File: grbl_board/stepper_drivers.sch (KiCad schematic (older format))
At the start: 44 parts

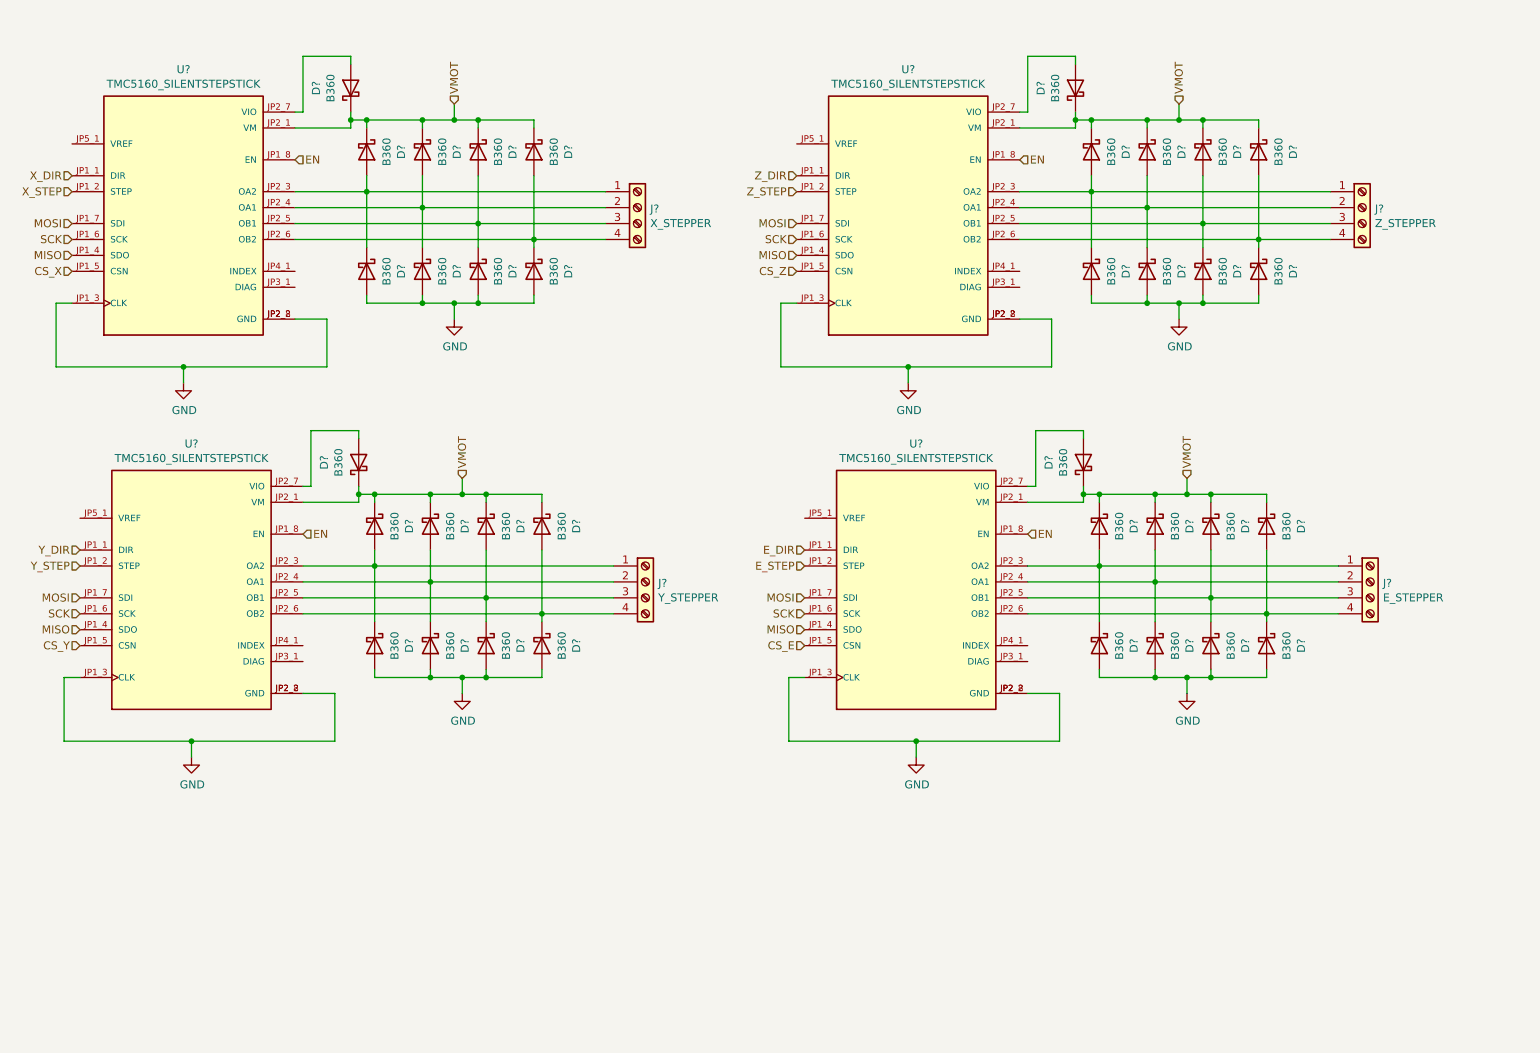
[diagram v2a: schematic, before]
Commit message: added some footprint associations
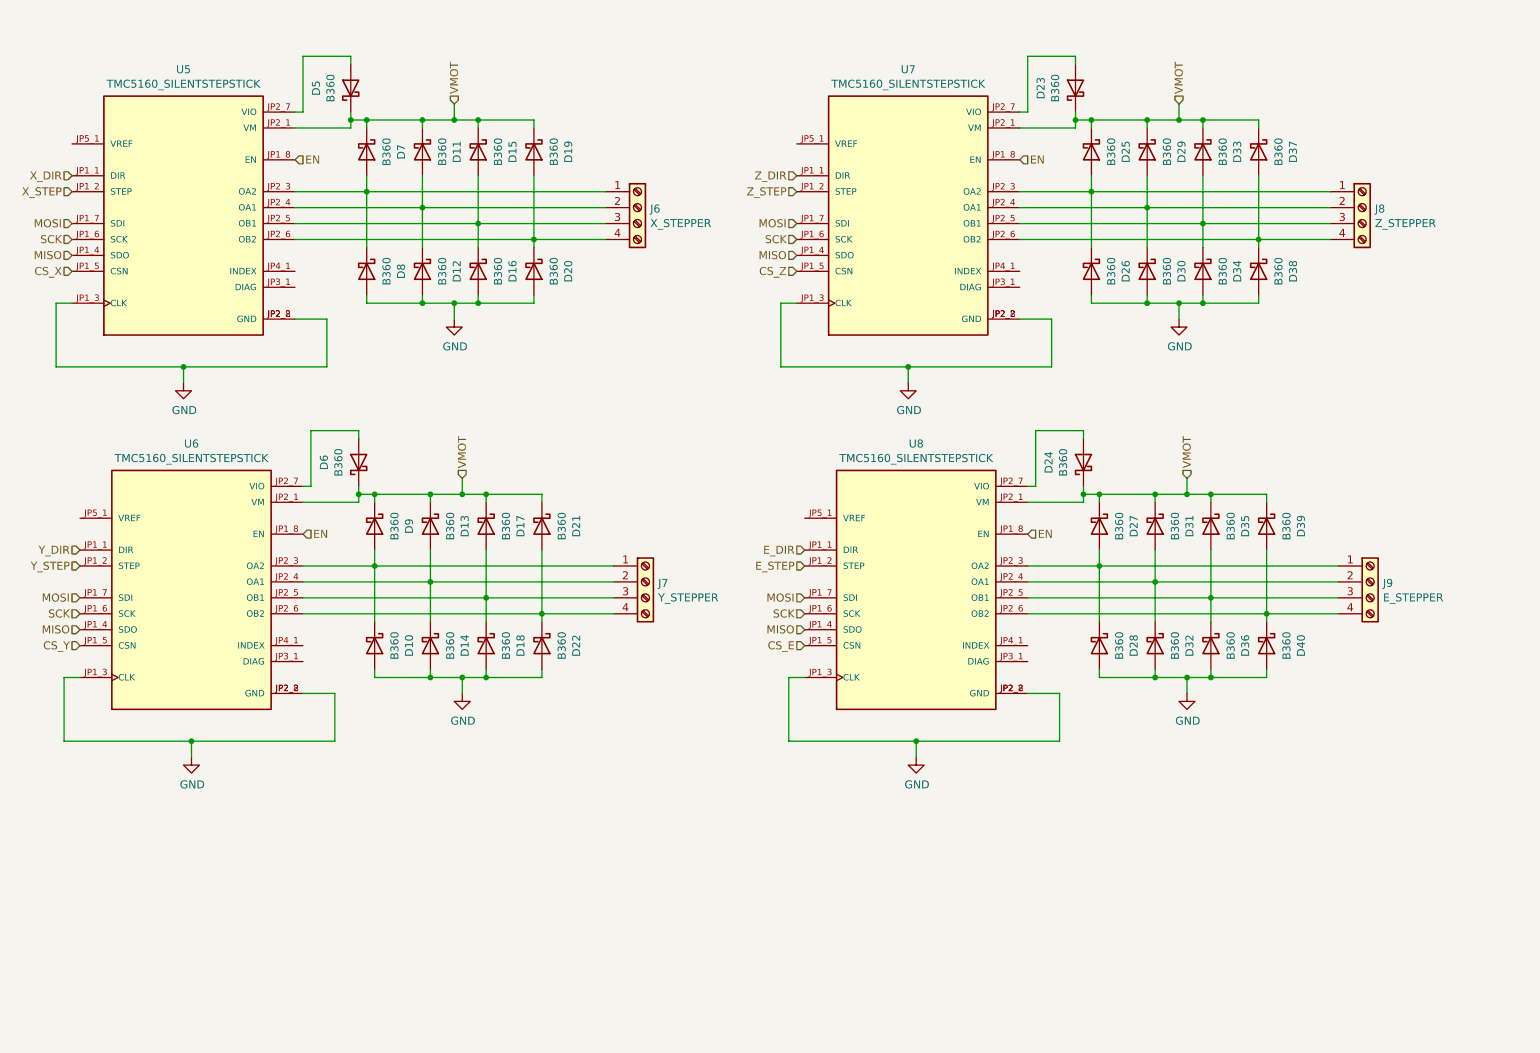
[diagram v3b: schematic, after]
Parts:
- J6, J7, J8, J9: renamed from J?; footprint (none) -> Connector_Phoenix_MC:PhoenixContact_MC_1,5_4-G-3.81_1x04_P3.81mm_Horizontal; Digikey Part No. (none) -> ED2810-ND
- gave numbers to parts that had none: 40

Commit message: complete footprint associations
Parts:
- U5, U6, U7, U8: Digikey Part No. (none) -> 1460-TMC5160SILENTSTEPSTICK-ND
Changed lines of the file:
@@
 F 1 "TMC5160_SILENTSTEPSTICK" H 2150 2676 50  0000 C CNN
 F 2 "grbl_board:TMC5160_SILENTSTEPSTICK" H 2150 1900 50  0001 L BNN
-F 3 "" H 2150 1900 50  0001 L BNN
+F 3 "https://www.trinamic.com/fileadmin/assets/Products/ICs_Documents/TMC5160_SilentStepStick_datasheet_Rev1.20.pdf" H 2150 1900 50  0001 L BNN
 F 4 "Manufacturer Recommendations" H 2150 1900 50  0001 L BNN "STANDARD"
 F 5 "N/A" H 2150 1900 50  0001 L BNN "MAXIMUM_PACKAGE_HEIGHT"
 F 6 "v11" H 2150 1900 50  0001 L BNN "PARTREV"
 F 7 "Trinamic" H 2150 1900 50  0001 L BNN "MANUFACTURER"
+F 8 "1460-TMC5160SILENTSTEPSTICK-ND" H 2150 1900 50  0001 C CNN "Digikey Part No."
 	1    2150 1900
 	1    0    0    -1
@@
 F 1 "TMC5160_SILENTSTEPSTICK" H 2200 5026 50  0000 C CNN
 F 2 "grbl_board:TMC5160_SILENTSTEPSTICK" H 2200 4250 50  0001 L BNN
-F 3 "" H 2200 4250 50  0001 L BNN
+F 3 "https://www.trinamic.com/fileadmin/assets/Products/ICs_Documents/TMC5160_SilentStepStick_datasheet_Rev1.20.pdf" H 2200 4250 50  0001 L BNN
 F 4 "Manufacturer Recommendations" H 2200 4250 50  0001 L BNN "STANDARD"
 F 5 "N/A" H 2200 4250 50  0001 L BNN "MAXIMUM_PACKAGE_HEIGHT"
 F 6 "v11" H 2200 4250 50  0001 L BNN "PARTREV"
 F 7 "Trinamic" H 2200 4250 50  0001 L BNN "MANUFACTURER"
+F 8 "1460-TMC5160SILENTSTEPSTICK-ND" H 2200 4250 50  0001 C CNN "Digikey Part No."
 	1    2200 4250
 	1    0    0    -1
@@
 F 1 "TMC5160_SILENTSTEPSTICK" H 6700 2676 50  0000 C CNN
 F 2 "grbl_board:TMC5160_SILENTSTEPSTICK" H 6700 1900 50  0001 L BNN
-F 3 "" H 6700 1900 50  0001 L BNN
+F 3 "https://www.trinamic.com/fileadmin/assets/Products/ICs_Documents/TMC5160_SilentStepStick_datasheet_Rev1.20.pdf" H 6700 1900 50  0001 L BNN
 F 4 "Manufacturer Recommendations" H 6700 1900 50  0001 L BNN "STANDARD"
 F 5 "N/A" H 6700 1900 50  0001 L BNN "MAXIMUM_PACKAGE_HEIGHT"
 F 6 "v11" H 6700 1900 50  0001 L BNN "PARTREV"
 F 7 "Trinamic" H 6700 1900 50  0001 L BNN "MANUFACTURER"
+F 8 "1460-TMC5160SILENTSTEPSTICK-ND" H 6700 1900 50  0001 C CNN "Digikey Part No."
 	1    6700 1900
 	1    0    0    -1
@@
 F 1 "TMC5160_SILENTSTEPSTICK" H 6750 5026 50  0000 C CNN
 F 2 "grbl_board:TMC5160_SILENTSTEPSTICK" H 6750 4250 50  0001 L BNN
-F 3 "" H 6750 4250 50  0001 L BNN
+F 3 "https://www.trinamic.com/fileadmin/assets/Products/ICs_Documents/TMC5160_SilentStepStick_datasheet_Rev1.20.pdf" H 6750 4250 50  0001 L BNN
 F 4 "Manufacturer Recommendations" H 6750 4250 50  0001 L BNN "STANDARD"
 F 5 "N/A" H 6750 4250 50  0001 L BNN "MAXIMUM_PACKAGE_HEIGHT"
 F 6 "v11" H 6750 4250 50  0001 L BNN "PARTREV"
 F 7 "Trinamic" H 6750 4250 50  0001 L BNN "MANUFACTURER"
+F 8 "1460-TMC5160SILENTSTEPSTICK-ND" H 6750 4250 50  0001 C CNN "Digikey Part No."
 	1    6750 4250
 	1    0    0    -1

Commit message: fixed mismatch for 6n137
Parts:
- D10, D11, D12, D13, D14, D15, D16, D17, D18, D19, D20, D21, D22, D23, D24, D25, D26, D27, D28, D29, D30, D31, D32, D33, D34, D35, D36, D37, D38, D39, D40, D5, D6, D7, D8, D9: footprint Diode_SMD:D_SMC -> Diode_SMD:D_SMA_Handsoldering; Digikey Part No. (none) -> CD214A-B360RCT-ND

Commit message: routing done
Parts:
- removed D23, D24, D6: B360, Diode_SMD:D_SMA_Handsoldering, symbol Diode:B360
- added HS1: heatsink_60x135mm, grbl_board:heatsink_60x135mm, symbol grbl_board:heatsink_60x135mm
- renumbered D11 to D10, D12 to D11, D13 to D12, D14 to D13, D15 to D14, D16 to D15, D17 to D16, D18 to D17, D19 to D18, D20 to D19, D21 to D20, D22 to D21, D25 to D22, D26 to D23, D27 to D24, D28 to D25, D29 to D26, D30 to D27, D31 to D28, D32 to D29, D33 to D30, D34 to D31, D35 to D32, D36 to D33, D37 to D34, D38 to D35, D39 to D36, D40 to D37, D7 to D6, D8 to D7, D9 to D8, D10 to D9
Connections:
- net +5V: now reaches D5.2 (A), U5.JP2_7 (VIO)
- net +5V: now also U6.JP2_7 (VIO), U7.JP2_7 (VIO), U8.JP2_7 (VIO)

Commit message: tidy up
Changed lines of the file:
@@
 	3900 4850 4050 4850
-Wire Wire Line
-	3250 3650 3250 3700
 Wire Wire Line
 	2900 3750 3250 3750
@@
 	3350 3700 3250 3700
 Connection ~ 3350 3700
-Connection ~ 3250 3700
 Wire Wire Line
 	3250 3700 3250 3750
@@
 	8400 2500 8550 2500
 Wire Wire Line
-	7750 1300 7750 1350
-Wire Wire Line
 	7400 1400 7750 1400
 Wire Wire Line
 	7850 1350 7750 1350
 Connection ~ 7850 1350
-Connection ~ 7750 1350
 Wire Wire Line
 	7750 1350 7750 1400
@@
 	8450 4850 8600 4850
 Wire Wire Line
-	7800 3650 7800 3700
-Wire Wire Line
 	7450 3750 7800 3750
 Wire Wire Line
 	7900 3700 7800 3700
 Connection ~ 7900 3700
-Connection ~ 7800 3700
 Wire Wire Line
 	7800 3700 7800 3750

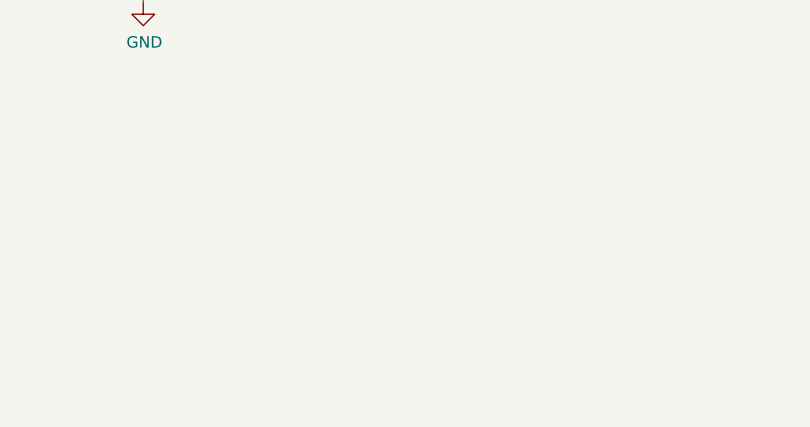
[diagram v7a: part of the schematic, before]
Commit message: added more filtering caps
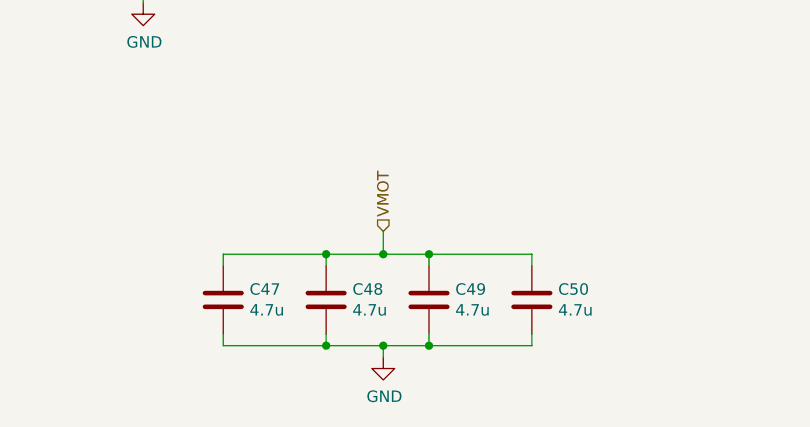
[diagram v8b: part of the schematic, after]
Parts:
- added C47, C48, C49, C50: 4.7u, Capacitor_SMD:C_1206_3216Metric_Pad1.33x1.80mm_HandSolder, symbol Device:C
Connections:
- net GND: now also C47.2, C48.2, C49.2, C50.2
- net VMOT: now also C47.1, C48.1, C49.1, C50.1
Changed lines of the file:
@@
 	1    0    0    -1
 $EndComp
+$Comp
+L Device:C C47
+U 1 1 6183BAC9
+P 2550 6650
+F 0 "C47" H 2665 6696 50  0000 L CNN
+F 1 "4.7u" H 2665 6605 50  0000 L CNN
+F 2 "Capacitor_SMD:C_1206_3216Metric_Pad1.33x1.80mm_HandSolder" H 2588 6500 50  0001 C CNN
+F 3 "http://www.samsungsem.com/kr/support/product-search/mlcc/CL31B475KBHVPNE.jsp" H 2550 6650 50  0001 C CNN
+F 4 "1276-6781-1-ND" H 2550 6650 50  0001 C CNN "Digikey Part No."
+	1    2550 6650
+	1    0    0    -1
+$EndComp
+$Comp
+L Device:C C48
+U 1 1 6183C6A1
+P 3000 6650
+F 0 "C48" H 3115 6696 50  0000 L CNN
+F 1 "4.7u" H 3115 6605 50  0000 L CNN
+F 2 "Capacitor_SMD:C_1206_3216Metric_Pad1.33x1.80mm_HandSolder" H 3038 6500 50  0001 C CNN
+F 3 "http://www.samsungsem.com/kr/support/product-search/mlcc/CL31B475KBHVPNE.jsp" H 3000 6650 50  0001 C CNN
+F 4 "1276-6781-1-ND" H 3000 6650 50  0001 C CNN "Digikey Part No."
+	1    3000 6650
+	1    0    0    -1
+$EndComp
+$Comp
+L Device:C C49
+U 1 1 61844DE6
+P 3450 6650
+F 0 "C49" H 3565 6696 50  0000 L CNN
+F 1 "4.7u" H 3565 6605 50  0000 L CNN
+F 2 "Capacitor_SMD:C_1206_3216Metric_Pad1.33x1.80mm_HandSolder" H 3488 6500 50  0001 C CNN
+F 3 "http://www.samsungsem.com/kr/support/product-search/mlcc/CL31B475KBHVPNE.jsp" H 3450 6650 50  0001 C CNN
+F 4 "1276-6781-1-ND" H 3450 6650 50  0001 C CNN "Digikey Part No."
+	1    3450 6650
+	1    0    0    -1
+$EndComp
+$Comp
+L Device:C C50
+U 1 1 6184D473
+P 3900 6650
+F 0 "C50" H 4015 6696 50  0000 L CNN
+F 1 "4.7u" H 4015 6605 50  0000 L CNN
+F 2 "Capacitor_SMD:C_1206_3216Metric_Pad1.33x1.80mm_HandSolder" H 3938 6500 50  0001 C CNN
+F 3 "http://www.samsungsem.com/kr/support/product-search/mlcc/CL31B475KBHVPNE.jsp" H 3900 6650 50  0001 C CNN
+F 4 "1276-6781-1-ND" H 3900 6650 50  0001 C CNN "Digikey Part No."
+	1    3900 6650
+	1    0    0    -1
+$EndComp
+$Comp
+L power:GND #PWR077
+U 1 1 61855DAE
+P 3250 6900
+F 0 "#PWR077" H 3250 6650 50  0001 C CNN
+F 1 "GND" H 3255 6727 50  0000 C CNN
+F 2 "" H 3250 6900 50  0001 C CNN
+F 3 "" H 3250 6900 50  0001 C CNN
+	1    3250 6900
+	1    0    0    -1
+$EndComp
+Text HLabel 3250 6350 1    50   Input ~ 0
+VMOT
+Wire Wire Line
+	3250 6350 3250 6450
+Wire Wire Line
+	3250 6450 3000 6450
+Wire Wire Line
+	2550 6450 2550 6500
+Wire Wire Line
+	2550 6800 2550 6850
+Wire Wire Line
+	2550 6850 3000 6850
+Wire Wire Line
+	3900 6850 3900 6800
+Wire Wire Line
+	3900 6500 3900 6450
+Wire Wire Line
+	3900 6450 3450 6450
+Connection ~ 3250 6450
+Wire Wire Line
+	3450 6500 3450 6450
+Connection ~ 3450 6450
+Wire Wire Line
+	3450 6450 3250 6450
+Wire Wire Line
+	3000 6500 3000 6450
+Connection ~ 3000 6450
+Wire Wire Line
+	3000 6450 2550 6450
+Wire Wire Line
+	3000 6850 3000 6800
+Connection ~ 3000 6850
+Wire Wire Line
+	3000 6850 3250 6850
+Wire Wire Line
+	3450 6850 3450 6800
+Connection ~ 3450 6850
+Wire Wire Line
+	3450 6850 3900 6850
+Wire Wire Line
+	3250 6900 3250 6850
+Connection ~ 3250 6850
+Wire Wire Line
+	3250 6850 3450 6850
 $EndSCHEMATC
